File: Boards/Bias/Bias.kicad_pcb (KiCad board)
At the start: 2 copper layers, 80 x 50 mm, 36 parts, among them P1 CONN_12V, P2 CONN_R, U1 LM339

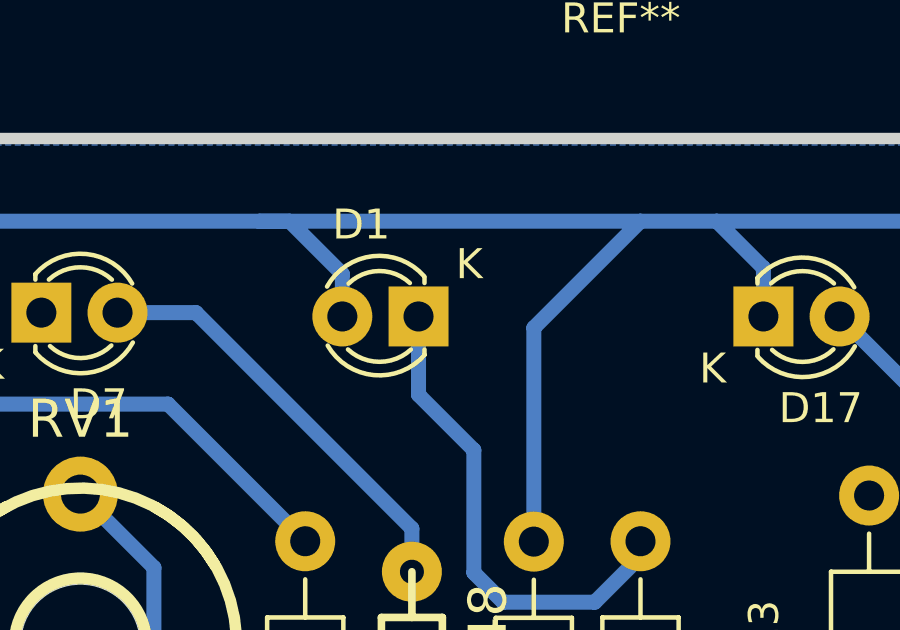
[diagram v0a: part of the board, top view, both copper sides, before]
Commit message: New Layout of Bias Board
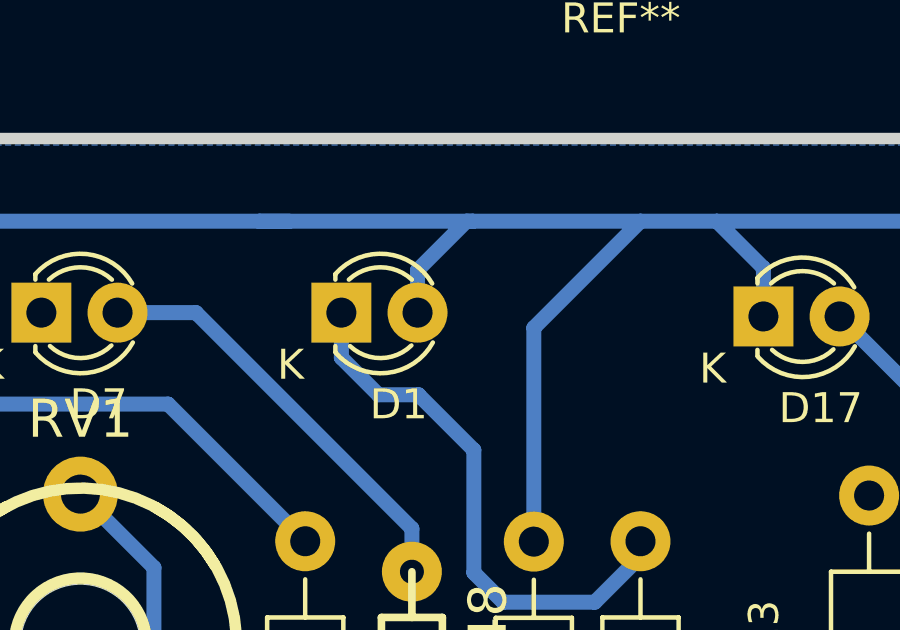
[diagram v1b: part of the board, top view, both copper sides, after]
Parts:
- moved D1 2.58 mm to (171.9, 68.1), turned to 0 degrees
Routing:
- net Net-(D1-Pad1): track 16.4 -> 18.4 mm
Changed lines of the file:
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@@
     (thickness 1.6)
     (drawings 2)
-    (tracks 194)
+    (tracks 198)
     (zones 0)
     (modules 36)
@@
       (padsonsilk false)
       (subtractmaskfromsilk false)
-      (outputformat 1)
+      (outputformat 4)
       (mirror false)
       (drillshape 0)
@@
   )
   (module LEDs:LED-3MM (layer F.Cu)
-    (at 174.465 68.199 180)
+    (at 171.892 68.072)
     (descr "LED 3mm round vertical")
     (tags "LED  3mm round vertical")
-    (fp_text reference D1 (at 1.91 3.06 180) (layer F.SilkS)
-      (effects (font (size 1 1) (thickness 0.15)))
-    )
-    (fp_text value LED_ZV_R1 (at 1.3 -2.9 180) (layer F.Fab)
+    (fp_text reference D1 (at 1.91 3.06) (layer F.SilkS)
+      (effects (font (size 1 1) (thickness 0.15)))
+    )
+    (fp_text value LED_ZV_R1 (at 1.3 -2.9) (layer F.Fab)
       (effects (font (size 1 1) (thickness 0.15)))
     )
@@
     (fp_arc (start 1.311 0.034) (end 3.051 0.994) (angle 110) (layer F.SilkS) (width 0.15))
     (fp_arc (start 1.301 0.034) (end 2.335 1.094) (angle 87.5) (layer F.SilkS) (width 0.15))
-    (fp_text user K (at -1.69 1.74 180) (layer F.SilkS)
-      (effects (font (size 1 1) (thickness 0.15)))
-    )
-    (pad 1 thru_hole rect (at 0 0 270) (size 2 2) (drill 1.00076) (layers *.Cu *.Mask F.SilkS)
+    (fp_text user K (at -1.69 1.74) (layer F.SilkS)
+      (effects (font (size 1 1) (thickness 0.15)))
+    )
+    (pad 1 thru_hole rect (at 0 0 90) (size 2 2) (drill 1.00076) (layers *.Cu *.Mask F.SilkS)
       (net 5 "Net-(D1-Pad1)"))
-    (pad 2 thru_hole circle (at 2.54 0 180) (size 2 2) (drill 1.00076) (layers *.Cu *.Mask F.SilkS)
+    (pad 2 thru_hole circle (at 2.54 0) (size 2 2) (drill 1.00076) (layers *.Cu *.Mask F.SilkS)
       (net 1 +12V))
     (model LEDs.3dshapes/LED-3MM.wrl
@@
     (effects (font (size 1.5 1.5) (thickness 0.3)) (justify mirror))
   )
+  (segment (start 169.164 65.024) (end 176.276 65.024) (width 0.5) (layer B.Cu) (net 1))
+  (segment (start 176.276 65.024) (end 181.864 65.024) (width 0.5) (layer B.Cu) (net 1))
+  (segment (start 174.432 68.072) (end 174.432 66.657787) (width 0.5) (layer B.Cu) (net 1))
+  (segment (start 174.432 66.657787) (end 176.065787 65.024) (width 0.5) (layer B.Cu) (net 1))
+  (segment (start 176.065787 65.024) (end 176.276 65.024) (width 0.5) (layer B.Cu) (net 1))
   (segment (start 216.916 75.692) (end 209.423 68.199) (width 0.5) (layer B.Cu) (net 1) (status 10))
   (segment (start 209.423 68.199) (end 208.408 68.199) (width 0.5) (layer B.Cu) (net 1) (status 20))
@@
   (segment (start 185.961 68.199) (end 185.961 66.581) (width 0.5) (layer B.Cu) (net 1) (status 10))
   (segment (start 185.961 66.581) (end 184.404 65.024) (width 0.5) (layer B.Cu) (net 1))
-  (segment (start 171.925 68.199) (end 171.925 66.784787) (width 0.5) (layer B.Cu) (net 1) (status 10))
   (segment (start 170.164213 65.024) (end 169.164 65.024) (width 0.5) (layer B.Cu) (net 1))
-  (segment (start 171.925 66.784787) (end 170.164213 65.024) (width 0.5) (layer B.Cu) (net 1))
   (segment (start 153.439 65.024) (end 169.164 65.024) (width 0.5) (layer B.Cu) (net 1))
   (segment (start 151.891 68.072) (end 151.891 66.572) (width 0.5) (layer B.Cu) (net 1) (status 10))
@@
   (segment (start 159.0421 95.805937) (end 157.988 94.751837) (width 0.5) (layer B.Cu) (net 1))
   (segment (start 157.988 94.751837) (end 157.988 93.472) (width 0.5) (layer B.Cu) (net 1) (status 20))
-  (segment (start 169.164 65.024) (end 181.864 65.024) (width 0.5) (layer B.Cu) (net 1))
   (segment (start 178.308 75.7047) (end 178.308 68.58) (width 0.5) (layer B.Cu) (net 1) (status 10))
   (segment (start 178.308 68.58) (end 181.864 65.024) (width 0.5) (layer B.Cu) (net 1))
@@
   (segment (start 186.944 104.648) (end 186.944 108.204) (width 0.5) (layer B.Cu) (net 4) (status 30))
   (segment (start 202.692 104.14) (end 202.692 101.6) (width 0.5) (layer B.Cu) (net 4) (status 30))
+  (segment (start 174.465 70.809) (end 173.129 70.809) (width 0.5) (layer B.Cu) (net 5))
+  (segment (start 173.129 70.809) (end 171.892 69.572) (width 0.5) (layer B.Cu) (net 5))
+  (segment (start 171.892 69.572) (end 171.892 68.072) (width 0.5) (layer B.Cu) (net 5))
   (segment (start 176.309067 72.653067) (end 174.465 70.809) (width 0.5) (layer B.Cu) (net 5))
-  (segment (start 174.465 70.809) (end 174.465 68.199) (width 0.5) (layer B.Cu) (net 5) (status 20))
   (segment (start 176.309067 76.741067) (end 177.292 77.724) (width 0.5) (layer B.Cu) (net 5))
   (segment (start 176.309067 72.653067) (end 176.309067 76.741067) (width 0.5) (layer B.Cu) (net 5))

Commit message: Work in Progress
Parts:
- moved C4 2.16 mm to (186.9, 106.0)
- moved R17 1.78 mm to (186.9, 102.9)
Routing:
- net Net-(D15-Pad2): track 18.3 -> 19.8 mm
- net Net-(D11-Pad1): track 33.4 -> 32.1 mm
- net Net-(C4-Pad1): track 35.6 -> 36.5 mm
- net Net-(D23-Pad1): track 13.7 -> 12.9 mm
- net /UG_R1: track 31.5 -> 32.4 mm
- net Net-(D1-Pad1): track 18.4 -> 17.6 mm
- net /BIAS_R2: track 6.34 -> 5.61 mm
- net +12V: track 188.0 -> 187.2 mm
- net /UG_R2: track 70.6 -> 70.1 mm

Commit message: Work in Progress
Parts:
- added C3: 100nF, Capacitors_THT:C_Disc_D3.0mm_W2.0mm_P2.50mm, F.Cu at (208.3, 102.6)
- added C5: 100nF, Capacitors_THT:C_Disc_D3.0mm_W2.0mm_P2.50mm, F.Cu at (211.3, 102.6)
- added R2: 0R, Measurement_Points:Test_Point_2Pads, F.Cu at (169.2, 104.6)
- C1, C2, C4: footprint Capacitors_ThroughHole:C_Disc_D3_P2.5 -> Capacitors_THT:C_Disc_D3.0mm_W2.0mm_P2.50mm
- D1, D13, D17, D19, D5, D7: footprint LEDs:LED-3MM -> LEDs:LED_D3.0mm
- D11, D15, D18, D23, D3, D6: footprint w_pth_diodes:diode_do35 -> Diodes_THT:D_DO-35_SOD27_P10.16mm_Horizontal
- D25: footprint w_pth_diodes:diode_do41 -> Diodes_THT:D_DO-41_SOD81_P10.16mm_Horizontal
- P1: footprint Sockets_Mini-Universal:MiniUniversalMate-N-LokSocket_2PinHorizontal -> Connectors_Molex:Molex_KK-6410-02_02x2.54mm_Straight; moved to B.Cu
- P2: footprint Pin_Headers:Pin_Header_Angled_2x03 -> Pin_Headers:Pin_Header_Straight_2x03_Pitch2.54mm
- R1, R11, R13, R15, R17, R19, R21, R22, R23, R24, R3, R5, R7, R9: footprint Resistors_ThroughHole:Resistor_Horizontal_RM10mm -> Resistors_THT:R_Axial_DIN0207_L6.3mm_D2.5mm_P10.16mm_Horizontal
- moved C1 33.2 mm to (191.0, 97.0), turned to 90 degrees
- moved D15 6.43 mm to (206.8, 94.0)
- moved D23 6.37 mm to (206.8, 90.9)
- moved D25 5.08 mm to (142.7, 75.7)
- moved D18 4.83 mm to (209.8, 75.7)
- moved D6 4.83 mm to (174.2, 75.7)
- moved P1 2.27 mm to (156.0, 100.1)
- moved D11 1.83 mm to (186.9, 94.0)
- moved D3 1.61 mm to (186.9, 90.9)
- moved C4 1.56 mm to (188.5, 106.0), turned to 0 degrees
- moved R13 1.52 mm to (189.5, 85.9)
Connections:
- P2 pad 4: GND -> GNDS
- R13 pad 2: GND -> GNDS
- R9 pad 2: GND -> GNDS
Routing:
- net GNDS: track 0.00 -> 12.2 mm
- net Net-(D23-Pad1): track 12.9 -> 9.58 mm
- net +12V: track 187.2 -> 190.5 mm
- net REF_L: track 90.5 -> 93.2 mm
- net Net-(D15-Pad1): track 17.9 -> 15.7 mm
- net Net-(D11-Pad2): track 15.2 -> 13.5 mm
- net Net-(D15-Pad2): track 19.8 -> 18.2 mm
- net -60V: track 54.8 -> 53.7 mm
- net /BIAS_R1: track 16.7 -> 15.6 mm
- net Net-(D11-Pad1): track 32.1 -> 33.1 mm
- net Net-(C4-Pad1): track 36.5 -> 35.6 mm
- net Net-(R13-Pad1): track 5.28 -> 6.02 mm
- net /UG_R2: track 70.1 -> 70.8 mm
- net Net-(D18-Pad1): track 15.7 -> 15.1 mm
- net Net-(D6-Pad1): track 14.2 -> 13.7 mm

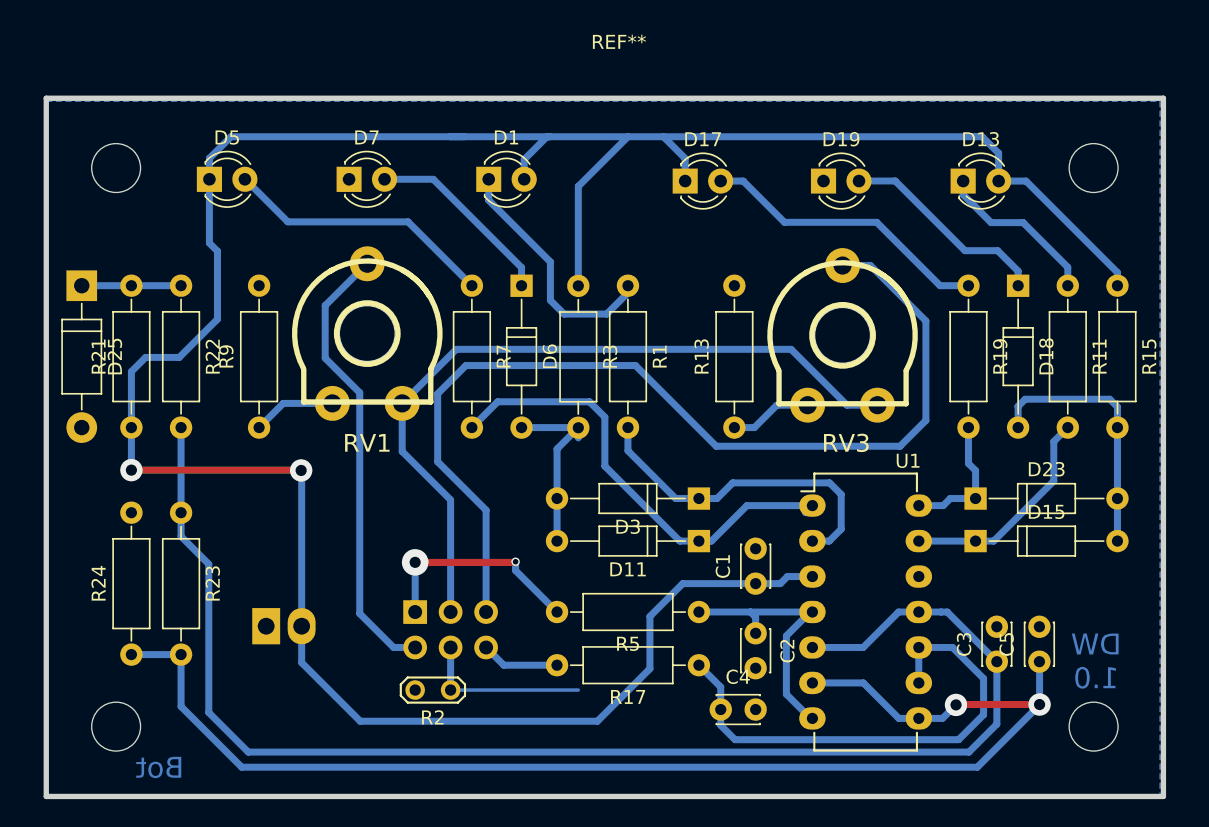
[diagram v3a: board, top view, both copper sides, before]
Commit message: Converted to Kicad 5.1 and Layout changes
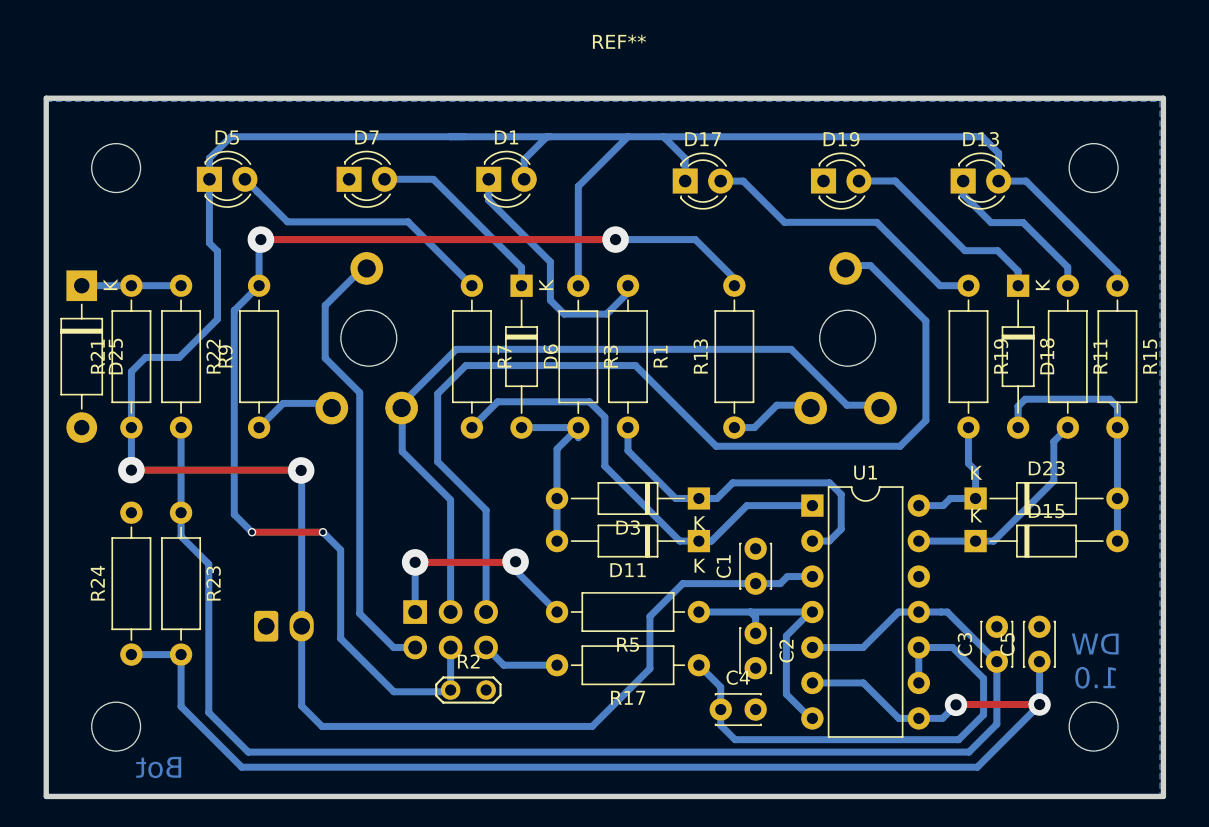
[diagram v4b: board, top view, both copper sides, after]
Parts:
- C1, C2, C3, C4, C5: footprint Capacitors_THT:C_Disc_D3.0mm_W2.0mm_P2.50mm -> Capacitor_THT:C_Disc_D3.0mm_W2.0mm_P2.50mm
- D1, D13, D17, D19, D5, D7: footprint LEDs:LED_D3.0mm -> LED_THT:LED_D3.0mm
- D11, D15, D18, D23, D3, D6: footprint Diodes_THT:D_DO-35_SOD27_P10.16mm_Horizontal -> Diode_THT:D_DO-35_SOD27_P10.16mm_Horizontal
- D25: footprint Diodes_THT:D_DO-41_SOD81_P10.16mm_Horizontal -> Diode_THT:D_DO-41_SOD81_P10.16mm_Horizontal
- P1: footprint Connectors_Molex:Molex_KK-6410-02_02x2.54mm_Straight -> Connector_Molex:Molex_KK-254_AE-6410-02A_1x02_P2.54mm_Vertical
- P2: footprint Pin_Headers:Pin_Header_Straight_2x03_Pitch2.54mm -> Connector_PinHeader_2.54mm:PinHeader_2x03_P2.54mm_Vertical
- R1, R11, R13, R15, R17, R19, R21, R22, R23, R24, R3, R5, R7, R9: footprint Resistors_THT:R_Axial_DIN0207_L6.3mm_D2.5mm_P10.16mm_Horizontal -> Resistor_THT:R_Axial_DIN0207_L6.3mm_D2.5mm_P10.16mm_Horizontal
- R2: footprint Measurement_Points:Test_Point_2Pads -> TestPoint:TestPoint_2Pads_Pitch2.54mm_Drill0.8mm
- RV1, RV3: footprint w_pth_resistors:trimmer_piher_pt10xv10 -> Potentiometer_THT:Potentiometer_Piher_PT-10-V10_Vertical_Hole; moved to B.Cu
- U1: footprint Housings_DIP:DIP-14_W7.62mm -> Package_DIP:DIP-14_W7.62mm
- moved RV1 5.91 mm to (160.7, 84.5), turned to 90 degrees
- moved RV3 5.69 mm to (194.9, 84.5), turned to 90 degrees
- turned R2 to 0 degrees
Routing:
- net GNDS: track 12.2 -> 83.6 mm, vias 0 -> 4
- net +12V: track 190.5 -> 192.6 mm

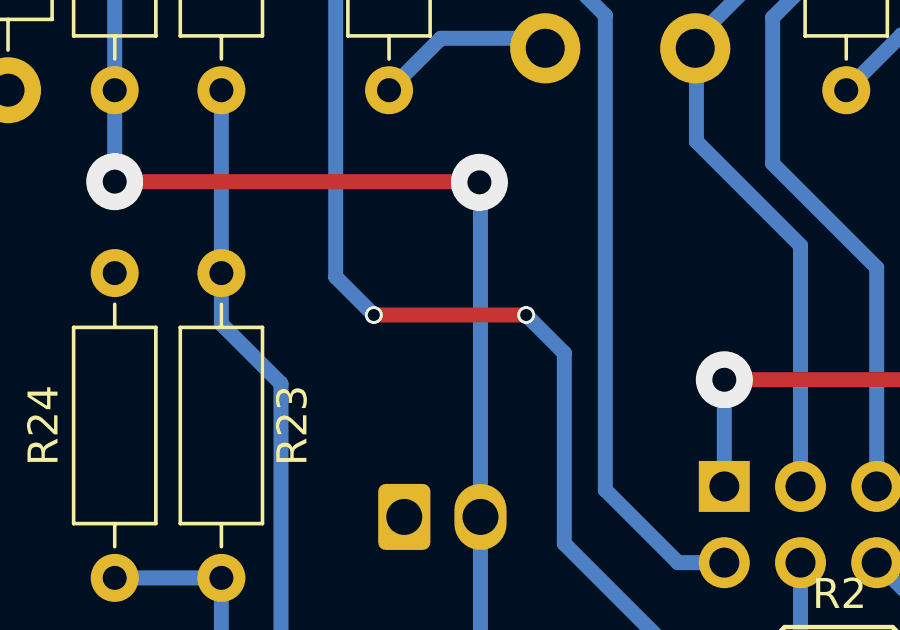
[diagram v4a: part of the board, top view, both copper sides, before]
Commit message: Layout changes after migrate to Kicad 5.1
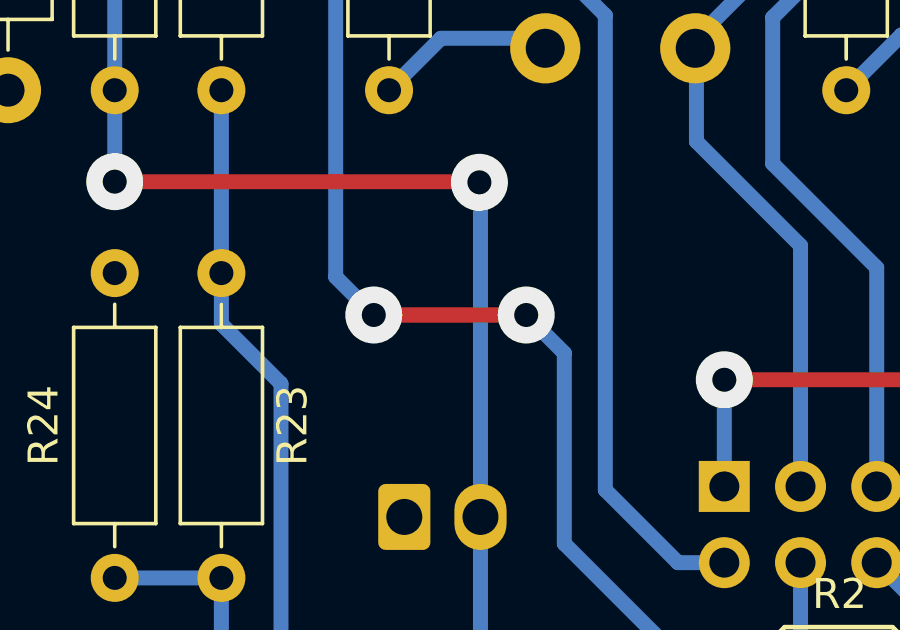
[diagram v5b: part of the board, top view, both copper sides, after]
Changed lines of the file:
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@@
   (segment (start 149.86 102.108) (end 146.304 102.108) (width 0.5) (layer B.Cu) (net 26) (status 30))
   (via (at 211.339822 105.685849) (size 1.6) (drill 0.8) (layers F.Cu B.Cu) (net 26))
-  (via (at 154.94 93.345) (size 0.6) (drill 0.4) (layers F.Cu B.Cu) (net 27))
-  (via (at 160.02 93.345) (size 0.6) (drill 0.4) (layers F.Cu B.Cu) (net 27))
+  (via (at 154.94 93.345) (size 1.9) (drill 0.8) (layers F.Cu B.Cu) (net 27))
+  (via (at 160.02 93.345) (size 1.9) (drill 0.8) (layers F.Cu B.Cu) (net 27))
   (segment (start 154.94 93.345) (end 160.02 93.345) (width 0.5) (layer F.Cu) (net 27))
   (segment (start 169.037 104.775) (end 169.164 104.648) (width 0.5) (layer B.Cu) (net 27))
